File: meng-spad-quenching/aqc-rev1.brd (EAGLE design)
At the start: 160 x 100 mm, 66 parts, among them IC1 ADCMP582, IC2 NC7SV74K8X, IC3 LT3032-5, IC4 PE29100, J1 VIN_LOGIC, M1 BSS806N, M2 EPC2040, M3 EPC2040, U1 SN65EPT21DGK, U2 TPS78233DDCT, U3 SN65EPT22DGK, X1 CONN_SPAD, X2 CONN_SCOPE_COMP, X3 CONN_SCOPE_RSHUNT, X4 CONN_VA_BIAS, X5 CONN_LATCH_IN

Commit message: Work on AQC rev. 1
Added buffer
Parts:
- removed M2, M3: EPC2040, meng:EPC2040
- added C26, C27, C29, C31: 10n, rcl:C0603
- added C28, C30, C32: 100n, rcl:C0603
- added C33: 33u, 25V, rcl:CT7343
- added IC5: OPA342, meng:SOT23-5
- added Q1, Q2, Q3, Q4, Q5: MMBTH81, transistor-pnp:SOT23-BEC
- added R17, R18, R19, R20, R21: 49R9, rcl:R0603
- added R22: 100R, rcl:R0603
- added R23, R24, R25, R26: 1k, rcl:R0603
- added R27: 470R, rcl:R0603
- added R28: 1k43, rcl:R0603
- added R29: 47R, rcl:R0603
- added T1, T2, T3, T4, T5, T6, T7: MMBTH10, transistor:SOT23-BEC
- C1: value 33p -> 100n; device rcl:C0805 -> rcl:C0603
- IC4: value PE29100 -> OPA342; device meng:PE29100 -> meng:SOT23-5
- R1: value 65k -> 470R; device rcl:R0805 -> rcl:R0603
- moved IC4 227.7 mm to (-97.8, -158.8)
- moved C1 221.7 mm to (-91.4, -141.0)
- moved R1 202.6 mm to (-91.4, -120.7)
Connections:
- new net DAC_CASCODE_IBIAS: IC5.3
- new net DAC_DIAMOND_IBIAS: IC4.3
- new net LOGIC_QUENCH_ATTEN: T6.B
- new net N$12: C26.1, Q3.C, R18.2, T2.B
- new net N$16: IC4.1, T3.B, T4.B
- new net N$18: Q4.C, Q5.B, R28.2
- new net N$19: C26.2, Q1.B, R20.1, T3.C
- new net N$20: R23.2, T3.E
- new net N$21: Q2.B, R21.1, T1.B
- new net N$22: R1.1, R21.2, T5.C
- new net N$23: IC4.4, R24.2, T4.E
- new net N$24: R27.2, T6.E, T7.C
- new net N$26: Q3.E, R25.1
- new net N$27: R28.1, T4.C
- new net N$29: Q4.E, R26.1
- new net N$30: IC5.1, T7.B
- new net N$31: Q3.B, Q4.B, Q5.E
- new net N$5: R17.2, T2.E
- new net PP_P15V0: C31.1, C32.1, C33.+, R1.2, R25.2, R26.2, T1.C, T2.C
- new net SPAD_PULLDN_SENSE: Q1.C, R22.2
- net GND: now also C1.2, C27.2, C28.2, C29.2, C30.2, C31.2, C32.2, C33.-, IC4.2, IC5.5, Q2.C, Q5.C, R22.1, R23.1, R24.1
- net N$11: now also Q2.E, R18.1; no longer M3.2, M3.5
- net N$13: now also R20.2, T1.E; no longer M2.3, M2.4, M2.6
- net N$14: now also Q1.E, R19.1; no longer M2.1
- net N$15: now also T5.E, T6.C; no longer M3.1
- net PP_N5V0: now also C29.1, C30.1, IC5.2, IC5.4, R27.1, R29.1, R29.2, T7.E
- net PP_P5V0: now also C1.1, C27.1, C28.1, IC4.5, T5.B
- net VA_FILT: no longer R1.2
- net VCOMP_IN: no longer C1.2
- net VSPAD: now also R17.1, R19.2; no longer C1.1, M2.2, M2.5, M3.3, M3.4, M3.6, R1.1

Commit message: Added LTC1711, upated one-shot design
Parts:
- removed C3: 33u, 25V, rcl:CT7343
- removed C4, C5: 10u, rcl:C1206
- removed R13: 50R, rcl:R0603
- removed RT2: 3269W-1-101LF, meng:3269W
- removed X4: CONN_VA_BIAS, con-coax:J502-ND-142-0711-871/876
- removed X5: CONN_LATCH_IN, con-coax:J502-ND-142-0711-871/876
- added C34, C41, C42: 10n, rcl:C0603
- added C35, C36: 100n, rcl:C0603
- added C37, C38, C39, C40: 10u, rcl:C1206
- added IC6: LTC1711, meng:US8_3.1MM_JDEC_MO-187
- added IC7: DS1100LU-20+, meng:US8_3.1MM_JDEC_MO-187
- added IC8: LT3032-15, meng:DFN14-4X3DE
- added R30: 100R, rcl:R0603
- added R31: 10k, rcl:R0603
- added R32, R33: DNP, rcl:R0603
- added TP5, TP6: TPTP20R, testpad:TP20R
- C2: value 100n -> 10n; device rcl:C0805 -> rcl:C0603
- R15: value 0R -> DNP
- R16: value DNP -> 470R
- R5: value 50R -> DNP; device rcl:R0805 -> rcl:R0603
- R7: value 470R -> 1k
- moved R12 364.5 mm to (-118.1, -276.9)
- moved R5 361.1 mm to (-118.1, -271.8)
- moved R2 355.7 mm to (-118.1, -266.7)
- moved C2 347.8 mm to (-118.1, -256.5)
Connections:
- net N$1 renamed HOLDOFF_TRIG
- removed net !LOGIC_QUENCH: IC2.3, M1.1
- removed net N$10: R13.1, U3.7, X5.1
- removed net VA_FILT: C2.1, C3.+, R5.1
- removed net VA_IN: R5.2, X4.1
- removed net VCOMP_IN: IC1.3, R2.2, R4.1
- removed net VREF: C21.1, IC1.2, R14.1, R7.2, RT1.2, RT1.3
- new net !ONE_SHOT_CLR: IC2.6, IC6.8
- new net BLANKING_LATCH_EN: R12.1, R2.1, R32.1, R33.1, R5.1, U3.7
- new net N$1: IC7.5, R33.2
- new net N$17: IC7.6, R12.2
- new net N$25: IC6.2, R30.1, R31.2
- new net N$28: IC7.2, R5.2
- new net N$32: IC7.7, R2.2
- new net N$33: C42.1, IC8.3
- new net N$34: C41.1, IC8.11
- new net N$36: IC3.10, IC3.12, IC3.14
- new net NC_!LOGIC_QUENCH: IC2.3
- new net ONE_SHOT_CAP: C20.1, M1.3, R16.1, R30.2
- new net ONE_SHOT_CLR: IC6.7, M1.1, R31.1
- new net ONE_SHOT_VREF: IC6.3
- new net PP_N15V0: C40.1, C41.2, IC3.6, IC3.9, IC8.7, TP5.TP
- new net VREF_AV_DET: C21.1, IC1.2, R14.2, R7.1, RT1.1
- net COMP_LE_N: now also U3.1; no longer U3.2
- net COMP_LE_P: now also U3.2; no longer U3.1
- net GND: now also C34.2, C35.2, C36.2, C37.2, C38.2, C39.2, C40.2, IC6.4, IC6.5, IC6.6, IC7.4, IC8.4, IC8.5, R14.1, RT1.2, RT1.3; no longer C3.-, C4.2, C5.2, R13.2, R14.2, R2.1, RT1.1, X4.G@1, X4.G@2, X4.G@3, X4.G@4, X5.G@1, X5.G@2, X5.G@3, X5.G@4
- net LOGIC_QUENCH: now also IC7.1; no longer RT2.1
- net N$6: no longer R12.2
- net N$7: now also IC7.3, R32.2; no longer C20.1, IC2.6, M1.3, R16.1, RT2.2, RT2.3
- net PP_N5V0: no longer R7.1
- net PP_NVIN: now also C38.1, IC8.6, IC8.9; no longer C5.1, IC3.6, IC3.9
- net PP_P15V0: now also C39.1, C42.2, IC8.1, TP6.TP
- net PP_P3V3: now also C2.1, C34.1, C35.1, C36.1, IC6.1, IC7.8; no longer R12.1
- net PP_P5V0: now also R7.2
- net PP_PVIN: now also C37.1, IC8.10, IC8.12, IC8.14; no longer C4.1, IC3.10, IC3.12, IC3.14
- net SPAD_PULLDN_SENSE: now also IC1.3, R4.1

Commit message: Started AQC rev. 1 layout, decided to make DACs external
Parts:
- added C3: 100n, rcl:C0603
- added C4: 10n, rcl:C0603
- added Q6: MMBTH81, transistor-pnp:SOT23-BEC
- added R13: 0R, rcl:R0603
- added R34, R35, R36, R37, R38, R39, R40, R41, R42, R43, R44, R45, R46: DNP, rcl:R0603
- added RT2, RT3, RT4: 3269W-1-102LF, meng:3269W
- added X4, X5, X6: CONN_VREF_ONE_SHOT_EXT, con-coax:J502-ND-142-0711-871/876
- IC6, IC7: device meng:US8_3.1MM_JDEC_MO-187 -> meng:MSOP8
- R22: value 100R -> 1k
- R29: value 47R -> 470R
- R7: value 1k -> DNP
- RT1: value 3269W-1-101LF -> 3269W-1-102LF
- moved IC8 481.7 mm to (120.7, 125.7)
- moved C38 475.5 mm to (101.6, 121.9)
- moved C39 475.5 mm to (106.7, 121.9)
- moved C40 475.5 mm to (111.8, 121.9)
- moved C37 475.5 mm to (110.5, 128.3)
- moved C41 475.5 mm to (108.0, 115.6)
- moved C42 475.5 mm to (113.0, 115.6)
- moved TP5 475.5 mm to (106.7, 109.2)
- moved TP6 475.5 mm to (111.8, 109.2)
- moved IC7 348.3 mm to (62.2, 45.7)
- moved C34 333.6 mm to (52.1, 57.1)
- moved C35 333.6 mm to (52.1, 52.1)
- moved R30 333.6 mm to (47.0, 47.0)
- moved R31 333.6 mm to (47.0, 41.9)
- moved IC6 332.5 mm to (45.7, 50.8)
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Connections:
- removed net DAC_CASCODE_IBIAS: IC5.3
- removed net DAC_DIAMOND_IBIAS: IC4.3
- removed net ONE_SHOT_VREF: IC6.3
- new net N$10: Q1.C, Q6.E
- new net VREF_CASCODE_IBIAS: IC5.3, R43.1, R44.1
- new net VREF_CASCODE_IBIAS_EXT: R43.2, X6.1
- new net VREF_CASCODE_IBIAS_INT: R44.2, R45.1, R46.2, RT4.2
- new net VREF_DIAMOND_IBIAS: IC4.3, R39.1, R40.1
- new net VREF_DIAMOND_IBIAS_EXT: R39.2, X5.1
- new net VREF_DIAMOND_IBIAS_INT: R40.2, R41.1, R42.2, RT3.2
- new net VREF_ONE_SHOT: C4.1, IC6.3, R35.1, R36.1
- new net VREF_ONE_SHOT_EXT: R35.2, X4.1
- new net VREF_ONE_SHOT_INT: R36.2, R37.1, R38.2, RT2.2
- net GND: now also C3.2, C4.2, R34.2, R37.2, R41.2, R45.2, RT2.3, RT3.3, RT4.3, X4.G@1, X4.G@2, X4.G@3, X4.G@4, X5.G@1, X5.G@2, X5.G@3, X5.G@4, X6.G@1, X6.G@2, X6.G@3, X6.G@4; no longer RT1.2
- net LOGIC_QUENCH: now also R13.2
- net LOGIC_QUENCH_ATTEN: now also R13.1, R34.1
- net PP_P3V3: now also R38.1, R46.1, RT2.1, RT4.1
- net PP_P5V0: now also C3.1, Q6.B, R42.1, RT1.1, RT3.1
- net SPAD_PULLDN_SENSE: now also Q6.C; no longer Q1.C
- net VREF_AV_DET: now also RT1.2; no longer RT1.1
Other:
- board size 160 x 100 mm -> 152.4 x 101.6 mm

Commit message: Added table of contents, work on AQC layout
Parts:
- added C5: 10n, rcl:C0603
- R11: value 50R -> 49R9
- R14, R3, R6, R7: device rcl:R0805 -> rcl:R0603
- X5: value CONN_VREF_ONE_SHOT_EXT -> CONN_VREF_DIAMOND_IBIAS_EXT
- X6: value CONN_VREF_ONE_SHOT_EXT -> CONN_VREF_CASCODE_IBIAS_EXT
- moved C33 320.0 mm to (16.5, 87.6), turned to 180 degrees
- moved C32 309.4 mm to (17.8, 81.3), turned to 180 degrees
- moved C31 306.3 mm to (21.6, 81.3), turned to 180 degrees
- moved C28 284.4 mm to (41.9, 78.1)
- moved C27 281.9 mm to (41.9, 80.3)
- moved IC4 280.2 mm to (41.9, 84.1)
- moved C30 262.4 mm to (21.6, 37.1)
- moved R29 261.6 mm to (29.2, 41.9)
- moved C29 259.9 mm to (21.6, 39.4)
- moved T7 254.6 mm to (25.4, 43.2)
- moved R28 252.5 mm to (21.6, 74.6), turned to 180 degrees
- moved Q5 246.4 mm to (15.6, 65.1), turned to 180 degrees
- moved IC5 245.0 mm to (25.7, 38.1), turned to 270 degrees
- moved R27 228.0 mm to (24.8, 50.2), turned to 90 degrees
- moved C1 227.5 mm to (24.8, 54.6), turned to 270 degrees
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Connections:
- net N$14: now also C5.2
- net N$5: now also C5.1
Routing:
- net GND: track 0.00 -> 31.0 mm, vias 0 -> 23
- net VREF_DIAMOND_IBIAS_INT: track 0.00 -> 22.6 mm
- net VREF_ONE_SHOT_INT: track 0.00 -> 22.2 mm
- net VREF_CASCODE_IBIAS_INT: track 0.00 -> 22.2 mm
- net PP_P5V0: track 0.00 -> 10.6 mm
- net VREF_AV_DET: track 0.00 -> 9.92 mm
- net N$12: track 0.00 -> 9.27 mm
- net VSPAD: track 0.00 -> 7.37 mm
- net PP_P15V0: track 0.00 -> 7.13 mm, vias 0 -> 5
- net VREF_ONE_SHOT_EXT: track 0.00 -> 7.06 mm
- net VREF_DIAMOND_IBIAS_EXT: track 0.00 -> 7.06 mm
- net VREF_CASCODE_IBIAS_EXT: track 0.00 -> 7.06 mm
- net N$31: track 0.00 -> 6.80 mm
- net N$21: track 0.00 -> 6.71 mm
- net PP_P3V3: track 0.00 -> 6.65 mm
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- added copper zone on layer 2, net GND
- added copper zone on layer 15, net PP_P15V0
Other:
- board size 152.4 x 101.6 mm -> 127 x 101.6 mm
- board text added: "EXT"
- board text added: "INT"

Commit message: More routing
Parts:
- removed R6: 49R9, rcl:R0603
- removed X3: CONN_SCOPE_RSHUNT, con-coax:J502-ND-142-0711-871/876
- added C43: 10n, rcl:C0603
- added C44: 100n, rcl:C0603
- added IC9: NC7WZ16P6X, meng:SC70-6L
- added TP4: TPTP20R, testpad:TP20R
- R4: value DNP -> 49R9
- X2: value CONN_SCOPE_COMP -> CONN_PHOTON_COUNTER
- moved X2 105.8 mm to (-20.3, 27.6), turned to 0 degrees
- moved C17 52.9 mm to (7.62, 24.8), turned to 180 degrees
- moved C16 52.5 mm to (7.62, 27.0), turned to 180 degrees
- moved R10 47.3 mm to (10.8, 24.8), turned to 270 degrees
- moved TP5 47.3 mm to (70.2, 54.3)
- moved TP6 46.8 mm to (64.8, 67.6)
- moved R11 46.1 mm to (7.62, 29.2), turned to 180 degrees
- moved R9 44.8 mm to (13.3, 24.8), turned to 270 degrees
- moved IC4 42.8 mm to (33.3, 42.2)
- moved C27 42.5 mm to (33.3, 38.7)
- moved C28 42.5 mm to (33.3, 36.5)
- moved R15 42.1 mm to (7.62, 31.4), turned to 0 degrees
- moved IC1 41.3 mm to (12.1, 29.2), turned to 270 degrees
- moved C9 41.2 mm to (64.8, 58.4), turned to 180 degrees
- moved C42 40.4 mm to (75.9, 58.4), turned to 180 degrees
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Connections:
- removed net N$36: IC3.10, IC3.12, IC3.14
- removed net VSCOPE_1: R4.2, X3.1
- new net N$35: IC5.4, R29.2, T7.E
- new net N$37: IC9.4, IC9.6, R4.2
- net GND: now also C43.2, C44.2, IC9.2; no longer X3.G@1, X3.G@2, X3.G@3, X3.G@4
- net HOLDOFF_TRIG: no longer R6.2
- net LOGIC_QUENCH: now also IC9.1, IC9.3
- net N$2: now also R4.1; no longer R6.1
- net PP_N5V0: no longer IC5.4, R29.2, T7.E
- net PP_P15V0: now also IC3.10, IC3.12, IC3.14
- net PP_P3V3: now also C43.1, C44.1, IC9.5, TP4.TP
- net SPAD_PULLDN_SENSE: no longer R4.1
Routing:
- net GND: track 31.0 -> 74.3 mm, vias 23 -> 41
- net PP_N15V0: track 0.00 -> 25.2 mm
- net PP_PVIN: track 0.00 -> 23.9 mm
- net PP_P15V0: track 7.13 -> 28.0 mm
- net PP_N5V0: track 0.00 -> 9.11 mm
- net N$34: track 0.00 -> 6.14 mm, vias 0 -> 2
- net N$9: track 0.00 -> 6.14 mm, vias 0 -> 2
- net PP_NVIN: track 0.00 -> 5.14 mm
- net LOGIC_QUENCH_ATTEN: track 0.00 -> 4.53 mm
- net PP_P5V0: track 10.6 -> 14.9 mm
- net N$24: track 2.54 -> 6.03 mm
- net N$3: track 0.00 -> 3.31 mm
- net SPAD_PULLDN_SENSE: track 0.21 -> 3.28 mm
- net N$10: track 0.00 -> 2.64 mm
- net COMP_Q_P: track 0.00 -> 2.57 mm
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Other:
- board size 127 x 101.6 mm -> 127 x 76.2 mm
- board text added: "GND"
- board text added: "N15V0"
- board text added: "N5V0"
- board text added: "P15V0"
- board text added: "P3V3"
- board text added: "P5V0"

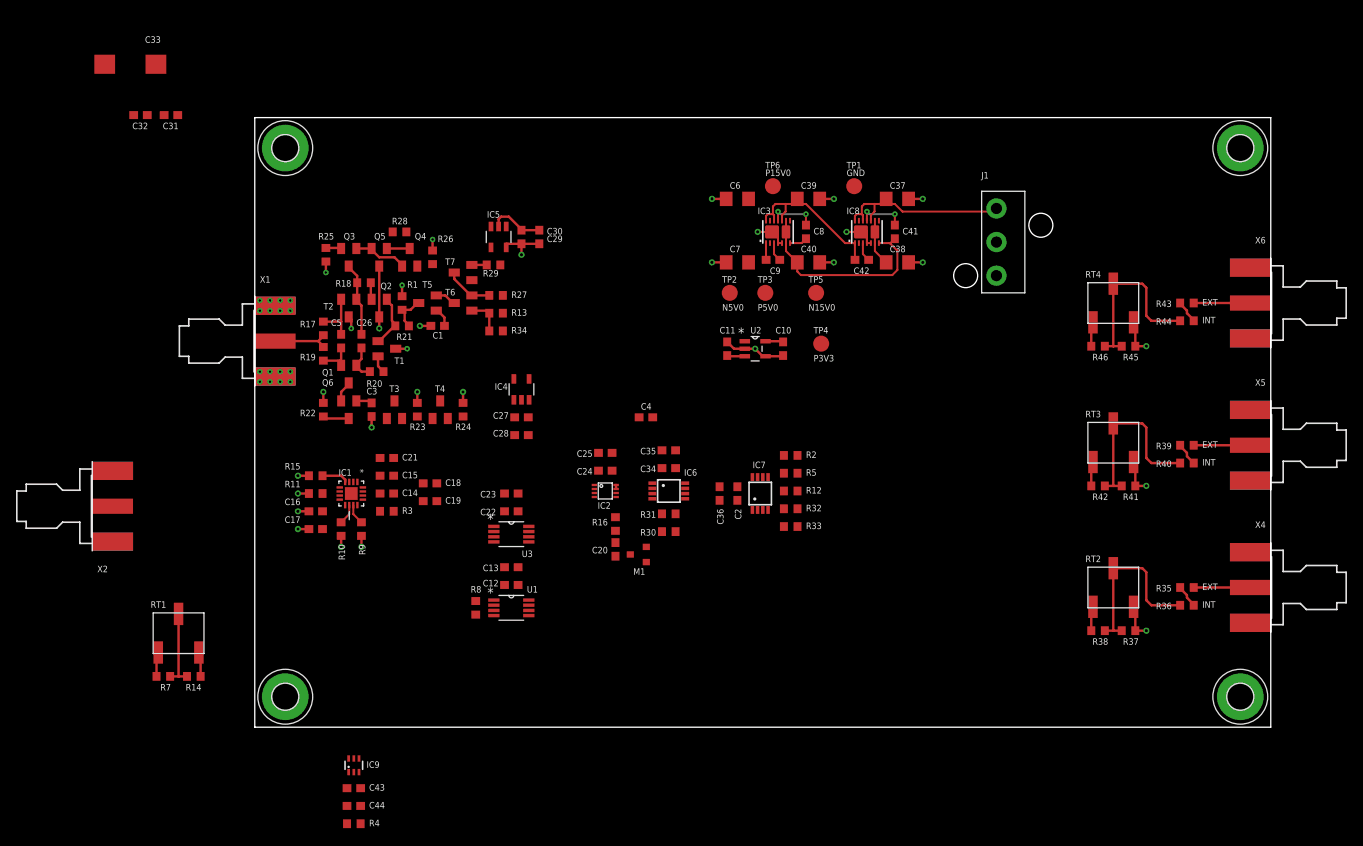
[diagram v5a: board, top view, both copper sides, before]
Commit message: Added forced quenching input, finalized connector placement in layout
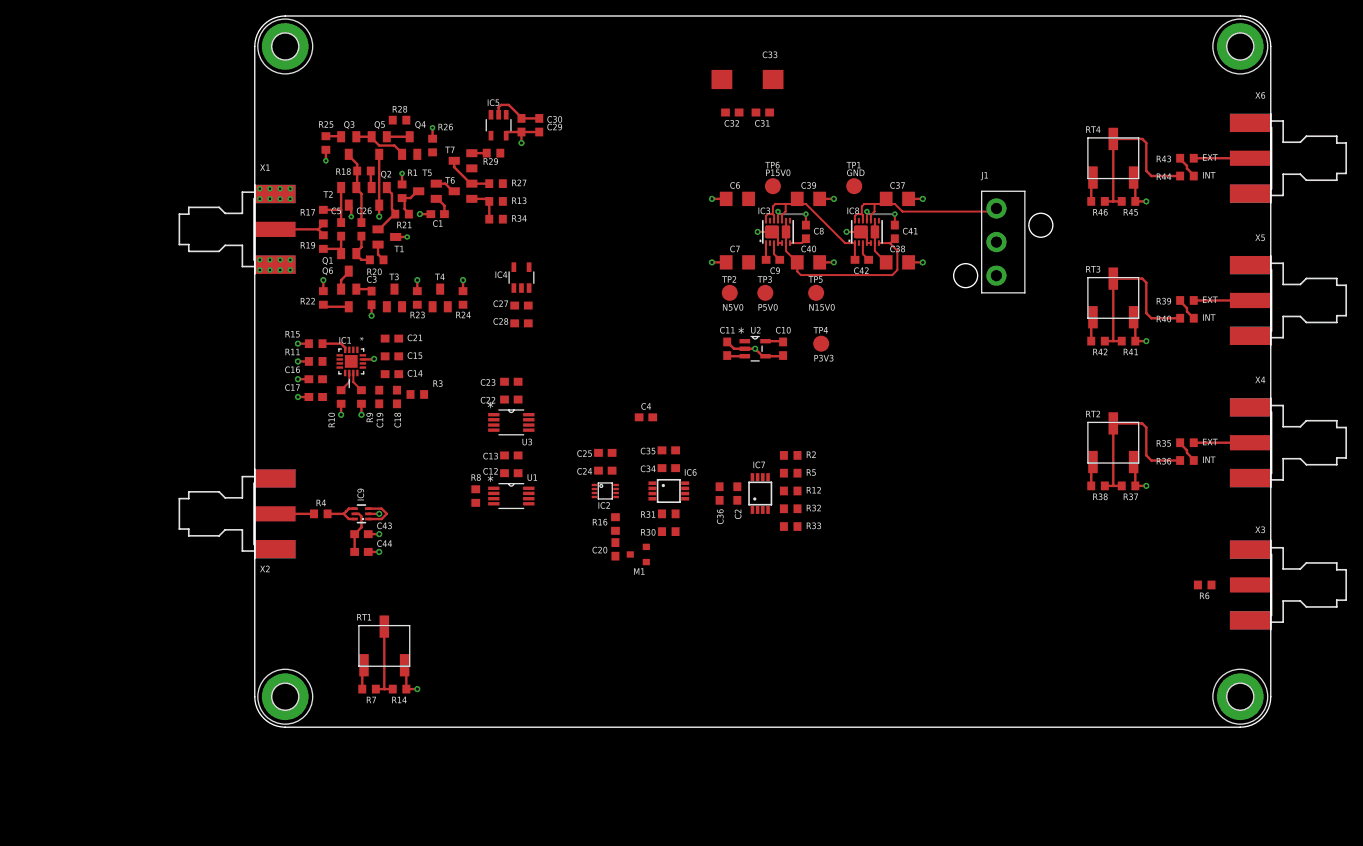
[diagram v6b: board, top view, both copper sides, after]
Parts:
- added R6: 49R9, rcl:R0603
- added X3: CONN_FORCE_QUENCH, con-coax:J502-ND-142-0711-871/876
- moved C33 77.2 mm to (61.6, 81.0)
- moved C31 74.0 mm to (63.5, 76.8)
- moved C32 74.0 mm to (59.7, 76.8)
- moved R4 39.0 mm to (8.26, 26.7)
- moved C43 31.8 mm to (13.3, 24.1)
- moved C44 31.8 mm to (13.3, 21.9)
- moved IC9 31.4 mm to (13.3, 26.7), turned to 90 degrees
- moved R14 25.8 mm to (18.1, 4.76)
- moved R7 25.8 mm to (14.3, 4.76)
- moved RT1 25.8 mm to (16.2, 10.2)
- moved X2 20.3 mm to (0.00, 26.7)
- moved R35 18.1 mm to (116.5, 35.6)
- moved R37 18.1 mm to (109.2, 30.2)
- moved R38 18.1 mm to (105.4, 30.2)
- moved R39 18.1 mm to (116.5, 53.3)
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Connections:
- new net !FORCE_QUENCH: IC2.7, R6.1, X3.1
- net GND: now also X3.G@1, X3.G@2, X3.G@3, X3.G@4
- net PP_P3V3: now also R6.2; no longer IC2.7
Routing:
- net GND: track 74.3 -> 81.2 mm, vias 41 -> 46
- net N$37: track 0.00 -> 5.29 mm
- net PP_P3V3: track 8.88 -> 14.2 mm
- net LOGIC_QUENCH: track 0.00 -> 5.19 mm
- net N$2: track 0.00 -> 4.84 mm
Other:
- board size 127 x 76.2 mm -> 127 x 88.9 mm
